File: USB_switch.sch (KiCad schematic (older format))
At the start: 16 parts, among them Q1 Q_PMOS_GSD, SW1 SW_SPDT

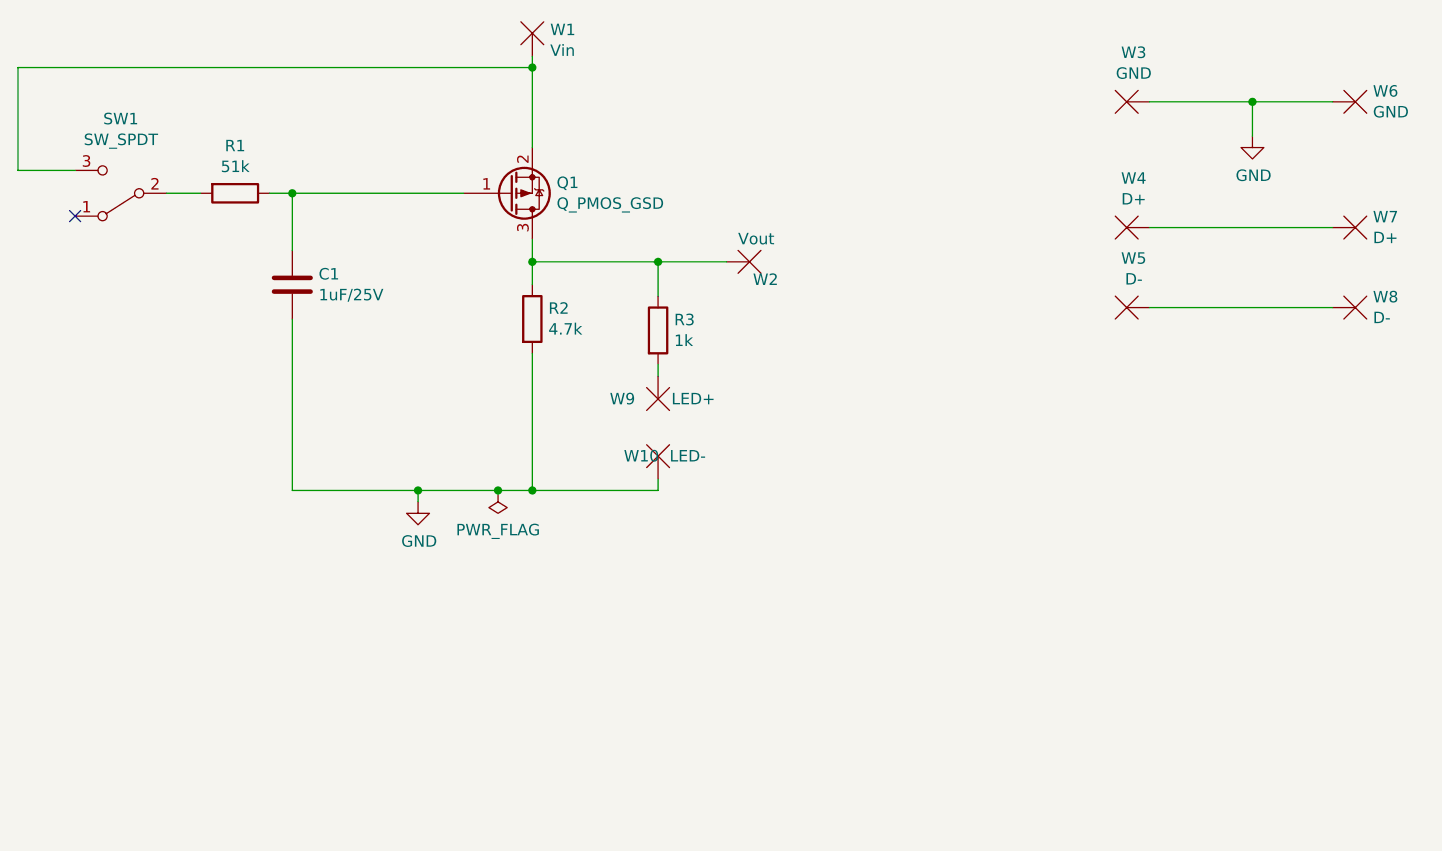
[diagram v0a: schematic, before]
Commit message: Routing done with USB connector.
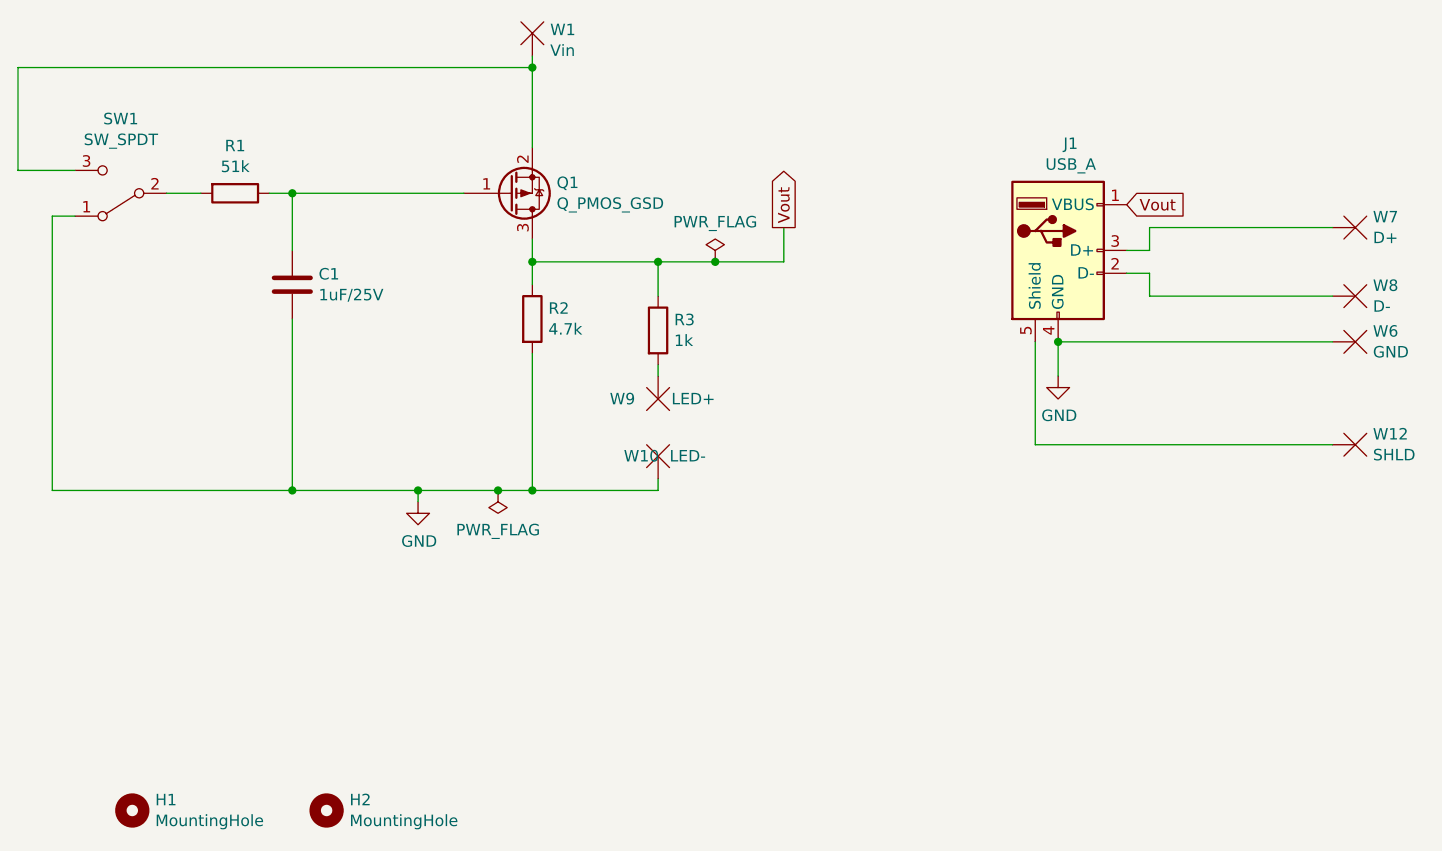
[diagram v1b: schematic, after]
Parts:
- removed W2: Vout, Pads:wirepad_hole_2.2x1mm, symbol pads:WirePad
- removed W3: GND, Pads:wirepad_hole_2.2x1mm, symbol pads:WirePad
- removed W4: D+, Pads:wirepad_hole_2.2x1mm, symbol pads:WirePad
- removed W5: D-, Pads:wirepad_hole_2.2x1mm, symbol pads:WirePad
- added H1, H2: MountingHole, MountingHole:MountingHole_2.7mm_M2.5_Pad, symbol Mechanical:MountingHole
- added J1: USB_A, Connectors_custom:USB_A_Receptacle_Horizontal, symbol Connector:USB_A
- added W12: SHLD, Pads:wirepad_SMD_2.2x4mm, symbol pads:WirePad
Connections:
- net GND: now also SW1.1 (A), J1.4 (GND)
- net Vout: now reaches Q1.3 (D), R2.1, R3.1
- net Vout: now also J1.1 (VBUS)
- net at W7.1: now also J1.3 (D+)
- net at W8.1: now also J1.2 (D-)
- new net: J1.5 (Shield), W12.1
- no-connect marks 1 -> 0
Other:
- moved on the sheet: W6, W8
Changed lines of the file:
@@
 	-1   0    0    1
 $EndComp
-NoConn ~ 2000 3300
 Wire Wire Line
 	2000 3100 1750 3100
@@
 	3500 4500 3500 4550
 Connection ~ 3500 4500
-Wire Wire Line
-	4000 3500 4550 3500
 Connection ~ 4000 3500
 Wire Wire Line
@@
 	-1   0    0    1
 $EndComp
-$Comp
-L pads:WirePad W2
-U 1 1 5BDF9C8C
-P 4850 3500
-F 0 "W2" V 4772 3385 50  0000 R CNN
-F 1 "Vout" V 4950 3450 50  0000 R CNN
-F 2 "Pads:wirepad_hole_2.2x1mm" H 4850 3500 50  0001 C CNN
-F 3 "" H 4850 3500 50  0001 C CNN
-	1    4850 3500
-	0    -1   -1   0
-$EndComp
 Wire Wire Line
 	2950 3200 3700 3200
-$Comp
-L pads:WirePad W3
-U 1 1 5BDFA0F9
-P 6700 2800
-F 0 "W3" V 6485 2731 50  0000 C CNN
-F 1 "GND" V 6576 2731 50  0000 C CNN
-F 2 "Pads:wirepad_hole_2.2x1mm" H 6700 2800 50  0001 C CNN
-F 3 "" H 6700 2800 50  0001 C CNN
-	1    6700 2800
-	0    1    1    0
-$EndComp
 $Comp
 L pads:WirePad W6
 U 1 1 5BDFA250
-P 7500 2800
-F 0 "W6" V 7546 2623 50  0000 R CNN
-F 1 "GND" V 7455 2623 50  0000 R CNN
-F 2 "Pads:wirepad_hole_2.2x1mm" H 7500 2800 50  0001 C CNN
-F 3 "" H 7500 2800 50  0001 C CNN
-	1    7500 2800
-	0    -1   -1   0
-$EndComp
-Wire Wire Line
-	6700 2800 7150 2800
-$Comp
-L pads:WirePad W4
-U 1 1 5BDFA3F1
-P 6700 3350
-F 0 "W4" V 6485 3281 50  0000 C CNN
-F 1 "D+" V 6576 3281 50  0000 C CNN
-F 2 "Pads:wirepad_hole_2.2x1mm" H 6700 3350 50  0001 C CNN
-F 3 "" H 6700 3350 50  0001 C CNN
-	1    6700 3350
-	0    1    1    0
+P 7500 3850
+F 0 "W6" V 7546 3673 50  0000 R CNN
+F 1 "GND" V 7455 3673 50  0000 R CNN
+F 2 "Pads:wirepad_hole_2.2x1mm" H 7500 3850 50  0001 C CNN
+F 3 "" H 7500 3850 50  0001 C CNN
+	1    7500 3850
+	0    -1   -1   0
 $EndComp
 $Comp
@@
 $EndComp
 $Comp
-L pads:WirePad W5
-U 1 1 5BDFA4CB
-P 6700 3700
-F 0 "W5" V 6485 3631 50  0000 C CNN
-F 1 "D-" V 6576 3631 50  0000 C CNN
-F 2 "Pads:wirepad_hole_2.2x1mm" H 6700 3700 50  0001 C CNN
-F 3 "" H 6700 3700 50  0001 C CNN
-	1    6700 3700
-	0    1    1    0
-$EndComp
-$Comp
 L pads:WirePad W8
 U 1 1 5BDFA513
-P 7500 3700
-F 0 "W8" V 7546 3523 50  0000 R CNN
-F 1 "D-" V 7455 3523 50  0000 R CNN
-F 2 "Pads:wirepad_hole_2.2x1mm" H 7500 3700 50  0001 C CNN
-F 3 "" H 7500 3700 50  0001 C CNN
-	1    7500 3700
+P 7500 3650
+F 0 "W8" V 7546 3473 50  0000 R CNN
+F 1 "D-" V 7455 3473 50  0000 R CNN
+F 2 "Pads:wirepad_hole_2.2x1mm" H 7500 3650 50  0001 C CNN
+F 3 "" H 7500 3650 50  0001 C CNN
+	1    7500 3650
 	0    -1   -1   0
 $EndComp
@@
 	6700 3350 7500 3350
 Wire Wire Line
-	6700 3700 7500 3700
+	6700 3650 7500 3650
 Wire Wire Line
 	4000 2600 4000 2650
 Wire Wire Line
 	1750 3100 1750 2650
-Wire Wire Line
-	1750 2650 4000 2650
 Connection ~ 4000 2650
 Wire Wire Line
@@
 Connection ~ 4550 3500
 Wire Wire Line
-	4550 3500 4850 3500
+	4550 3500 4800 3500
 Wire Wire Line
 	4550 3950 4550 4000
@@
 $EndComp
 $Comp
-L power:GND #PWR?
+L power:GND #PWR0102
 U 1 1 5BE18B5C
-P 7150 2950
-F 0 "#PWR?" H 7150 2700 50  0001 C CNN
-F 1 "GND" H 7155 2777 50  0000 C CNN
-F 2 "" H 7150 2950 50  0001 C CNN
-F 3 "" H 7150 2950 50  0001 C CNN
-	1    7150 2950
-	1    0    0    -1
-$EndComp
-Wire Wire Line
-	7150 2950 7150 2800
-Connection ~ 7150 2800
-Wire Wire Line
-	7150 2800 7500 2800
+P 6300 4000
+F 0 "#PWR0102" H 6300 3750 50  0001 C CNN
+F 1 "GND" H 6305 3827 50  0000 C CNN
+F 2 "" H 6300 4000 50  0001 C CNN
+F 3 "" H 6300 4000 50  0001 C CNN
+	1    6300 4000
+	1    0    0    -1
+$EndComp
+Wire Wire Line
+	6300 4000 6300 3850
+Wire Wire Line
+	6300 3850 7500 3850
+$Comp
+L pads:WirePad W12
+U 1 1 5BE1974B
+P 7500 4300
+F 0 "W12" V 7546 4123 50  0000 R CNN
+F 1 "SHLD" V 7455 4123 50  0000 R CNN
+F 2 "Pads:wirepad_SMD_2.2x4mm" H 7500 4300 50  0001 C CNN
+F 3 "" H 7500 4300 50  0001 C CNN
+	1    7500 4300
+	0    -1   -1   0
+$EndComp
+Wire Wire Line
+	6200 4300 7500 4300
+$Comp
+L Mechanical:MountingHole H1
+U 1 1 5BE19D84
+P 2250 5900
+F 0 "H1" H 2350 5946 50  0000 L CNN
+F 1 "MountingHole" H 2350 5855 50  0000 L CNN
+F 2 "MountingHole:MountingHole_2.7mm_M2.5_Pad" H 2250 5900 50  0001 C CNN
+F 3 "~" H 2250 5900 50  0001 C CNN
+	1    2250 5900
+	1    0    0    -1
+$EndComp
+$Comp
+L Mechanical:MountingHole H2
+U 1 1 5BE1A026
+P 3100 5900
+F 0 "H2" H 3200 5946 50  0000 L CNN
+F 1 "MountingHole" H 3200 5855 50  0000 L CNN
+F 2 "MountingHole:MountingHole_2.7mm_M2.5_Pad" H 3100 5900 50  0001 C CNN
+F 3 "~" H 3100 5900 50  0001 C CNN
+	1    3100 5900
+	1    0    0    -1
+$EndComp
+Wire Wire Line
+	2000 3300 1900 3300
+Wire Wire Line
+	1900 3300 1900 4500
+Wire Wire Line
+	1900 4500 2950 4500
+Connection ~ 2950 4500
+$Comp
+L Connector:USB_A J1
+U 1 1 5BE1CA77
+P 6300 3450
+F 0 "J1" H 6355 3917 50  0000 C CNN
+F 1 "USB_A" H 6355 3826 50  0000 C CNN
+F 2 "Connectors_custom:USB_A_Receptacle_Horizontal" H 6450 3400 50  0001 C CNN
+F 3 " ~" H 6450 3400 50  0001 C CNN
+F 4 "1642033" H 6300 3450 50  0001 C CNN "Farnell"
+F 5 "61400416021" H 6300 3450 50  0001 C CNN "Ref"
+	1    6300 3450
+	1    0    0    -1
+$EndComp
+Wire Wire Line
+	6700 3650 6700 3550
+Wire Wire Line
+	6700 3550 6600 3550
+Wire Wire Line
+	6700 3350 6700 3450
+Wire Wire Line
+	6700 3450 6600 3450
+Connection ~ 6300 3850
+Wire Wire Line
+	6200 4300 6200 3850
+Text GLabel 6600 3250 2    50   Input ~ 0
+Vout
+Text GLabel 5100 3350 1    50   Output ~ 0
+Vout
+Wire Wire Line
+	5100 3350 5100 3500
+$Comp
+L power:PWR_FLAG #FLG0102
+U 1 1 5BE2C45D
+P 4800 3500
+F 0 "#FLG0102" H 4800 3575 50  0001 C CNN
+F 1 "PWR_FLAG" H 4800 3674 50  0000 C CNN
+F 2 "" H 4800 3500 50  0001 C CNN
+F 3 "~" H 4800 3500 50  0001 C CNN
+	1    4800 3500
+	1    0    0    -1
+$EndComp
+Wire Wire Line
+	1750 2650 4000 2650
+Connection ~ 4800 3500
+Wire Wire Line
+	4800 3500 5100 3500
+Wire Wire Line
+	4000 3500 4550 3500
 $EndSCHEMATC
